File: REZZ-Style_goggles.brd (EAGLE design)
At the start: 65.5 x 65.5 mm, 77 parts

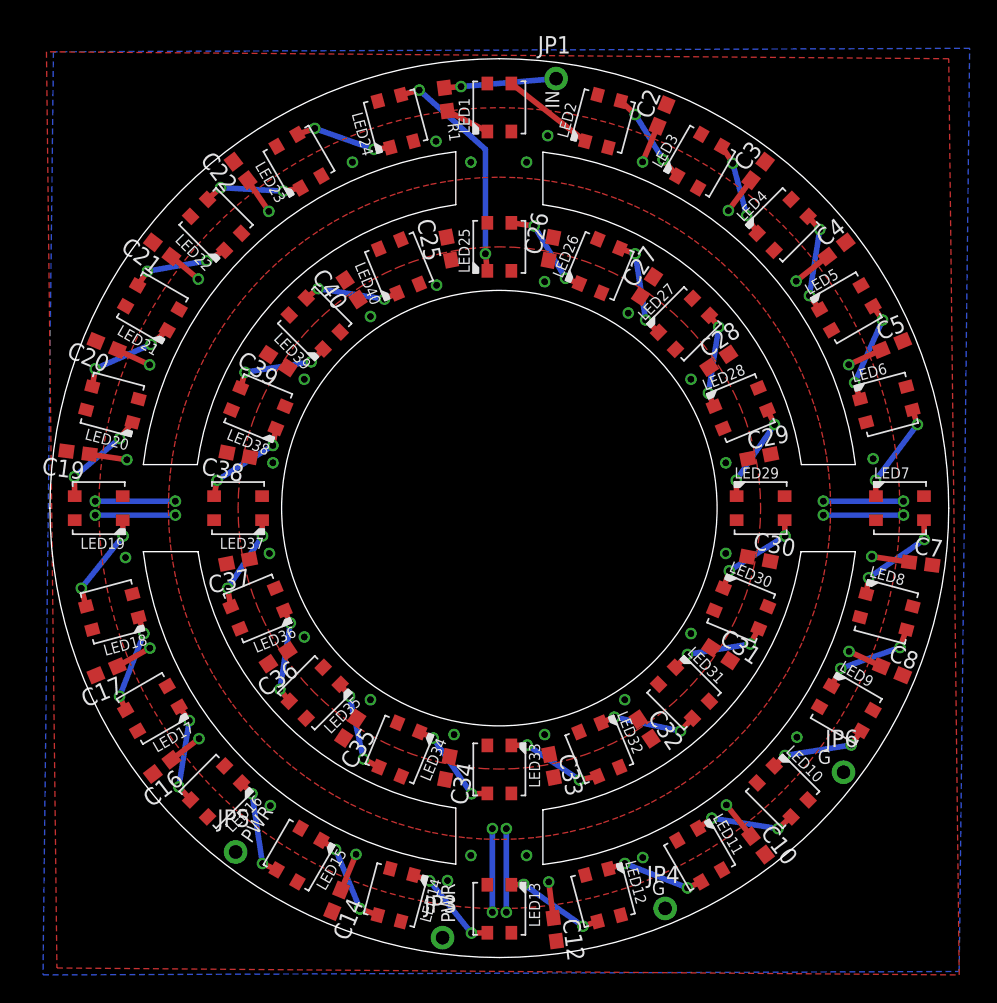
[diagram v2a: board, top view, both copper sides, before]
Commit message: inner ring completed
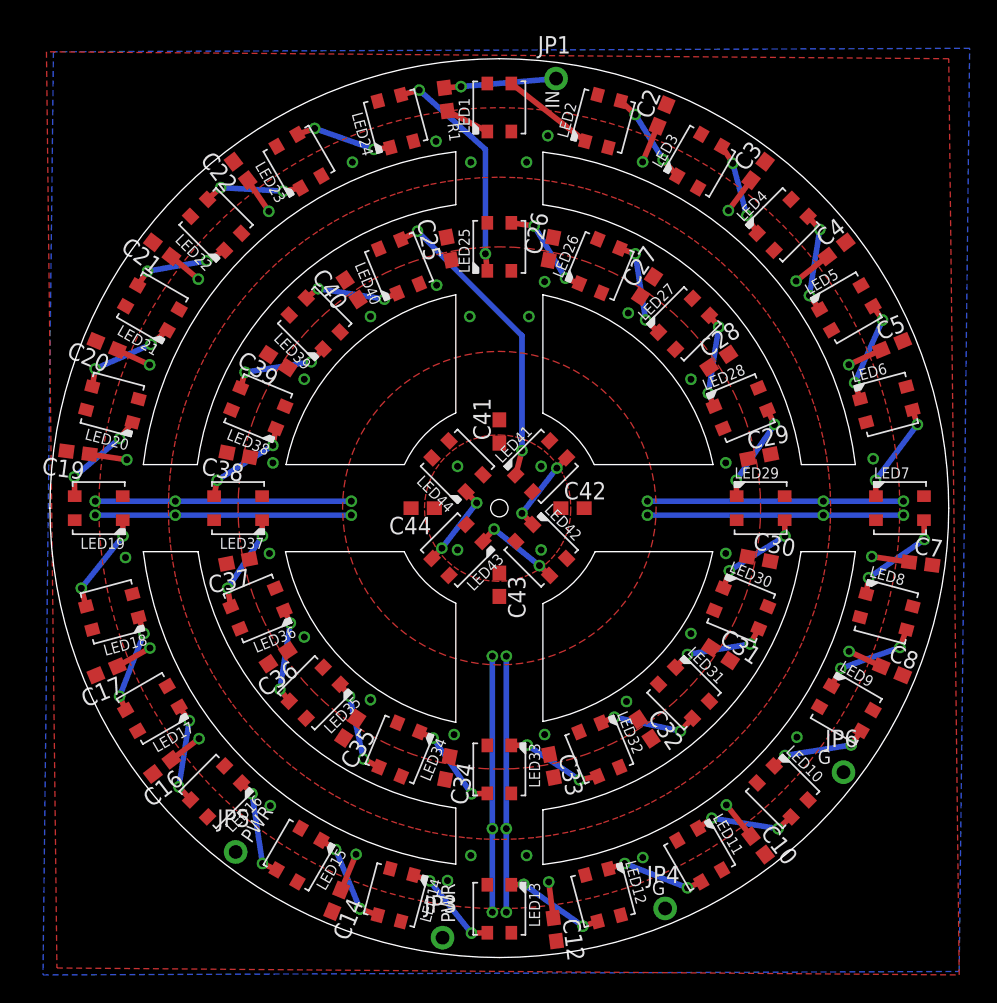
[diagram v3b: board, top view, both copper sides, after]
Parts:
- added C41, C42, C43, C44: (no value), rcl:C0603
- added LED41, LED42, LED43, LED44: WS2812B3535, adafruit:LED3535
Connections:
- new net N$42: LED40.3, LED41.1
- new net N$43: LED41.3, LED42.1
- new net N$44: LED42.3, LED43.1
- new net N$45: LED43.3, LED44.1
- net GND: now also C41.2, C42.2, C43.2, C44.2, LED41.4, LED42.4, LED43.4, LED44.4
- net VDD: now also C41.1, C42.1, C43.1, C44.1, LED41.2, LED42.2, LED43.2, LED44.2
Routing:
- net GND: track 35.6 -> 112.0 mm, vias 12 -> 18
- net N$42: track 0.00 -> 22.3 mm, vias 0 -> 2
- net N$44: track 0.00 -> 6.49 mm, vias 0 -> 2
- net N$45: track 0.00 -> 6.32 mm, vias 0 -> 2
- net N$43: track 0.00 -> 6.32 mm, vias 0 -> 2
- net VDD: vias 44 -> 50
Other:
- outline, holes or cut-outs redrawn
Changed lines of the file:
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@@
 <setting verticaltext="up"/>
 </settings>
-<grid distance="0.01" unitdist="inch" unit="inch" style="lines" multiple="5" display="yes" altdistance="0.1" altunitdist="inch" altunit="inch"/>
+<grid distance="0.005" unitdist="inch" unit="inch" style="lines" multiple="5" display="yes" altdistance="0.1" altunitdist="inch" altunit="inch"/>
 <layers>
 <layer number="1" name="Top" color="4" fill="1" visible="yes" active="yes"/>
@@
 <text x="59.4106" y="17.5514" size="1.016" layer="22" ratio="10" rot="MR0">GND</text>
 <text x="17.4244" y="11.4554" size="1.016" layer="22" ratio="10" rot="MR0">PWR +5V</text>
-<circle x="33.02" y="35.56" radius="15.875" width="0.0254" layer="20"/>
 <wire x1="11.049" y1="32.385" x2="7.0612" y2="32.385" width="0.0254" layer="20"/>
 <wire x1="55.0164" y1="32.385" x2="58.9788" y2="32.385" width="0.0254" layer="20"/>
@@
 <wire x1="29.845" y1="9.6012" x2="7.0612" y2="32.385" width="0.0254" layer="20" curve="-76.053667"/>
 <wire x1="29.845" y1="13.6906" x2="11.049" y2="32.385" width="0.0254" layer="20" curve="-73.212053"/>
+<hole x="33.02" y="35.56" drill="1.27"/>
+<wire x1="17.4625" y1="38.735" x2="26.0858" y2="38.735" width="0.0254" layer="20"/>
+<wire x1="48.6029" y1="38.735" x2="39.9415" y2="38.735" width="0.0254" layer="20"/>
+<wire x1="48.5775" y1="32.385" x2="40.005" y2="32.385" width="0.0254" layer="20"/>
+<wire x1="17.4244" y1="32.385" x2="26.0858" y2="32.385" width="0.0254" layer="20"/>
+<wire x1="29.845" y1="51.1175" x2="29.845" y2="42.5069" width="0.0254" layer="20"/>
+<wire x1="36.195" y1="51.1175" x2="36.195" y2="42.4815" width="0.0254" layer="20"/>
+<wire x1="29.845" y1="19.939" x2="29.845" y2="28.6258" width="0.0254" layer="20"/>
+<wire x1="36.195" y1="20.0025" x2="36.195" y2="28.6004" width="0.0254" layer="20"/>
+<wire x1="17.4625" y1="38.735" x2="29.845" y2="51.1175" width="0.0254" layer="20" curve="-66.948628"/>
+<wire x1="26.0985" y1="38.735" x2="29.845" y2="42.5069" width="0.0254" layer="20" curve="-40.76551"/>
+<wire x1="36.195" y1="42.4815" x2="39.9415" y2="38.735" width="0.0254" layer="20" curve="-40.716676"/>
+<wire x1="40.005" y1="32.385" x2="36.195" y2="28.6004" width="0.0254" layer="20" curve="-41.277572"/>
+<wire x1="29.845" y1="28.6258" x2="26.0858" y2="32.385" width="0.0254" layer="20" curve="-40.906623"/>
+<wire x1="36.195" y1="51.1175" x2="48.6029" y2="38.735" width="0.0254" layer="20" curve="-66.904686"/>
+<wire x1="48.5775" y1="32.385" x2="36.195" y2="20.0025" width="0.0254" layer="20" curve="-66.975668"/>
+<wire x1="29.845" y1="19.939" x2="17.4244" y2="32.385" width="0.0254" layer="20" curve="-67.13794"/>
 </plain>
 <attributes>
@@
 <element name="C39" library="rcl" package="C0603" value="" x="16.891" y="46.2788" rot="R146.3"/>
 <element name="C40" library="rcl" package="C0603" value="" x="22.2504" y="51.4858" rot="R123.8"/>
+<element name="LED41" library="adafruit" package="LED3535" value="WS2812B3535" x="36.068" y="38.608" rot="R45"/>
+<element name="LED42" library="adafruit" package="LED3535" value="WS2812B3535" x="36.068" y="32.512" rot="R315"/>
+<element name="LED43" library="adafruit" package="LED3535" value="WS2812B3535" x="29.972" y="32.512" rot="R225"/>
+<element name="LED44" library="adafruit" package="LED3535" value="WS2812B3535" x="29.972" y="38.608" rot="R135"/>
+<element name="C41" library="rcl" package="C0603" value="" x="33.02" y="41.148" rot="R90"/>
+<element name="C42" library="rcl" package="C0603" value="" x="38.354" y="35.56"/>
+<element name="C43" library="rcl" package="C0603" value="" x="33.02" y="29.972" rot="R270"/>
+<element name="C44" library="rcl" package="C0603" value="" x="27.432" y="35.56" rot="R180"/>
 </elements>
 <signals>
@@
 <wire x1="3.556" y1="36.068" x2="9.398" y2="36.068" width="0.4064" layer="16"/>
 <wire x1="9.398" y1="35.052" x2="3.556" y2="35.052" width="0.4064" layer="16"/>
+<contactref element="LED41" pad="4"/>
+<contactref element="LED42" pad="4"/>
+<contactref element="LED43" pad="4"/>
+<contactref element="LED44" pad="4"/>
+<contactref element="C41" pad="2"/>
+<contactref element="C42" pad="2"/>
+<contactref element="C43" pad="2"/>
+<contactref element="C44" pad="2"/>
+<polygon width="0.4064" layer="1" rank="2">
+<vertex x="21.59" y="35.56" curve="-90"/>
+<vertex x="33.02" y="46.99" curve="-90"/>
+<vertex x="44.45" y="35.56" curve="-90"/>
+<vertex x="33.02" y="24.13" curve="-90"/>
+</polygon>
+<wire x1="32.512" y1="12.192" x2="32.512" y2="24.765" width="0.4064" layer="16"/>
+<wire x1="33.528" y1="12.192" x2="33.528" y2="24.765" width="0.4064" layer="16"/>
+<via x="32.512" y="24.765" extent="1-16" drill="0.5"/>
+<via x="33.528" y="24.765" extent="1-16" drill="0.5"/>
+<via x="43.815" y="35.052" extent="1-16" drill="0.5"/>
+<via x="43.815" y="36.068" extent="1-16" drill="0.5"/>
+<wire x1="56.642" y1="36.068" x2="43.815" y2="36.068" width="0.4064" layer="16"/>
+<wire x1="56.642" y1="35.052" x2="43.815" y2="35.052" width="0.4064" layer="16"/>
+<via x="22.225" y="36.068" extent="1-16" drill="0.5"/>
+<via x="22.225" y="35.052" extent="1-16" drill="0.5"/>
+<wire x1="9.398" y1="36.068" x2="22.225" y2="36.068" width="0.4064" layer="16"/>
+<wire x1="9.398" y1="35.052" x2="22.225" y2="35.052" width="0.4064" layer="16"/>
+<wire x1="36.686715625" y1="40.464153125" x2="39.204" y2="35.56" width="0" layer="19" extent="1-1"/>
 </signal>
 <signal name="VDD">
@@
 <wire x1="9.10994375" y1="53.906875" x2="11.0703375" y2="52.25923125" width="0.4064" layer="1"/>
 <wire x1="14.673121875" y1="59.470053125" x2="16.212059375" y2="57.2008" width="0.4064" layer="1"/>
-<polygon width="0.4064" layer="1" isolate="0.254">
+<polygon width="0.4064" layer="1" isolate="0.254" rank="3">
 <vertex x="13.97" y="35.56" curve="-90"/>
 <vertex x="33.02" y="54.61"/>
@@
 <via x="49.53" y="32.258" extent="1-16" drill="0.5"/>
 <via x="46.99" y="26.416" extent="1-16" drill="0.5"/>
-<via x="42.164" y="21.59" extent="1-16" drill="0.5"/>
+<via x="42.291" y="21.463" extent="1-16" drill="0.5"/>
 <via x="36.322" y="19.05" extent="1-16" drill="0.5"/>
 <via x="29.718" y="19.05" extent="1-16" drill="0.5"/>
@@
 <via x="30.942025" y="10.236453125" extent="1-16" drill="0.5"/>
 <via x="35.006025" y="10.236453125" extent="1-16" drill="0.5"/>
+<contactref element="LED41" pad="2"/>
+<contactref element="LED42" pad="2"/>
+<contactref element="LED43" pad="2"/>
+<contactref element="LED44" pad="2"/>
+<contactref element="C41" pad="1"/>
+<contactref element="C42" pad="1"/>
+<contactref element="C43" pad="1"/>
+<contactref element="C44" pad="1"/>
+<polygon width="0.4064" layer="1">
+<vertex x="27.559" y="35.56" curve="-90"/>
+<vertex x="32.893" y="40.894"/>
+<vertex x="33.02" y="40.894" curve="-90"/>
+<vertex x="38.227" y="35.687"/>
+<vertex x="38.227" y="35.56"/>
+<vertex x="38.227" y="35.433" curve="-90"/>
+<vertex x="33.02" y="30.226"/>
+<vertex x="32.893" y="30.226" curve="-90"/>
+</polygon>
+<via x="29.972" y="32.512" extent="1-16" drill="0.5"/>
+<via x="29.972" y="38.608" extent="1-16" drill="0.5"/>
+<via x="36.068" y="32.512" extent="1-16" drill="0.5"/>
+<via x="36.068" y="38.608" extent="1-16" drill="0.5"/>
+<via x="30.861" y="49.53" extent="1-16" drill="0.5"/>
+<via x="35.179" y="49.53" extent="1-16" drill="0.5"/>
 </signal>
 <signal name="N$12">
@@
 <wire x1="19.812" y1="51.562" x2="24.638" y2="50.8" width="0.4064" layer="16"/>
 </signal>
+<signal name="N$42">
+<contactref element="LED40" pad="3"/>
+<contactref element="LED41" pad="1"/>
+<via x="27.051" y="55.753" extent="1-16" drill="0.5"/>
+<via x="34.671" y="39.751" extent="1-16" drill="0.5"/>
+<wire x1="34.21184375" y1="37.98928125" x2="34.671" y2="39.751" width="0.4064" layer="1"/>
+<wire x1="25.843496875" y1="55.139234375" x2="27.051" y2="55.753" width="0.4064" layer="1"/>
+<wire x1="34.671" y1="39.751" x2="34.671" y2="48.133" width="0.4064" layer="16"/>
+<wire x1="34.671" y1="48.133" x2="27.051" y2="55.753" width="0.4064" layer="16"/>
+</signal>
+<signal name="N$43">
+<contactref element="LED41" pad="3"/>
+<contactref element="LED42" pad="1"/>
+<via x="34.671" y="35.179" extent="1-16" drill="0.5"/>
+<via x="37.211" y="38.481" extent="1-16" drill="0.5"/>
+<wire x1="37.211" y1="38.481" x2="34.671" y2="35.179" width="0.4064" layer="16"/>
+<wire x1="37.211" y1="38.481" x2="37.924153125" y2="39.226715625" width="0.4064" layer="1"/>
+<wire x1="34.671" y1="35.179" x2="35.44928125" y2="34.368153125" width="0.4064" layer="1"/>
+</signal>
+<signal name="N$44">
+<contactref element="LED42" pad="3"/>
+<contactref element="LED43" pad="1"/>
+<via x="35.941" y="31.369" extent="1-16" drill="0.5"/>
+<via x="32.639" y="34.036" extent="1-16" drill="0.5"/>
+<wire x1="35.941" y1="31.369" x2="32.639" y2="34.036" width="0.4064" layer="16"/>
+<wire x1="36.686715625" y1="30.65584375" x2="35.941" y2="31.369" width="0.4064" layer="1"/>
+<wire x1="31.828153125" y1="33.130715625" x2="32.639" y2="34.036" width="0.4064" layer="1"/>
+</signal>
+<signal name="N$45">
+<contactref element="LED43" pad="3"/>
+<contactref element="LED44" pad="1"/>
+<via x="28.829" y="32.639" extent="1-16" drill="0.5"/>
+<via x="31.369" y="35.941" extent="1-16" drill="0.5"/>
+<wire x1="28.829" y1="32.639" x2="31.369" y2="35.941" width="0.4064" layer="16"/>
+<wire x1="28.829" y1="32.639" x2="28.11584375" y2="31.89328125" width="0.4064" layer="1"/>
+<wire x1="30.590715625" y1="36.75184375" x2="31.369" y2="35.941" width="0.4064" layer="1"/>
+</signal>
 </signals>
